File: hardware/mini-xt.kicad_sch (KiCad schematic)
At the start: 0 parts

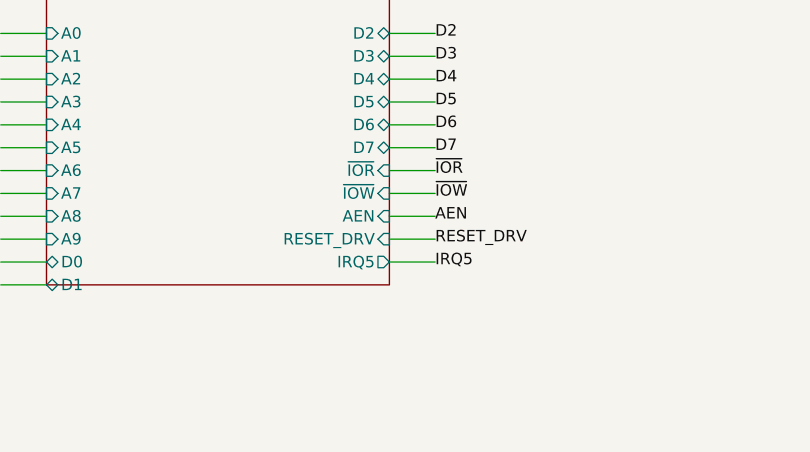
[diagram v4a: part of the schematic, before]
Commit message: Storage: on-board only, IRQ14-default strap; 16-bit IRQ collector
Remove card_storage (same rationale as COM/LPT/RTC -- the on-board sheet
carries the full jumper set; ~25-line wrapper, restorable from git).
Standalone PCBs remaining: video + the isatest jig.

- storage: JP3 IRQ strap -- 1-2 = IRQ14 (DEFAULT, the AT primary-IDE
  convention), 2-3 = IRQ5 (XT fallback; also the LPT alternate), open =
  polled. The '125 now drives STOR_IRQ into the strap, so the unselected
  line is untouched.
- bus_mcu: IRQ14 had no physical path into the soft-PIC, so the IRQ
  collector is now a cascaded pair of 74HCT165s (U19 IRQ10-15 -> U12
  IRQ2-9, net IRQ_CAS), with R19-R24 idle pull-downs and C18. Zero GPIO
  cost -- same IRQ_LOAD/IRQ_CLK/IRQ_SER, firmware shifts 16 bits. Also
  un-dangles the IRQ10-15 interface pins the sheet had declared since day
  one. IRQ10-15 are motherboard-internal (the 60-pin header carries only
  IRQ2-8).
- README: XT-IDE moves into the on-board peripherals list (all three
  straps + the shadow-loaded-BIOS note); motherboard is the third board;
  coexistence example now pairs the on-board XT-IDE with a real ISA IDE
  card at 0x320.
- Design doc: 4.3 card list, 10 JP3 strap + XTIDE UB IRQ-config note
  (was still "Poll or IRQ5"), 5.2 collector row, 14 IRQ table (IRQ14 no
  longer "spare"), 15 BOM row. Decisions logged in open-questions.md,
  questions-storage.md, questions-bus_mcu.md.

Verified: motherboard + both cards rebuild with zero structural ERC;
netlist shows /IRQ14 = {JP3, pull-down, U19 collector input} spanning
storage<->bus_mcu, IRQ_CAS = U19.Q7 -> U12.DS, and /IRQ5 still carrying
sidecar + LPT strap + collector.

Co-Authored-By: Claude Fable 5 <noreply@anthropic.com>
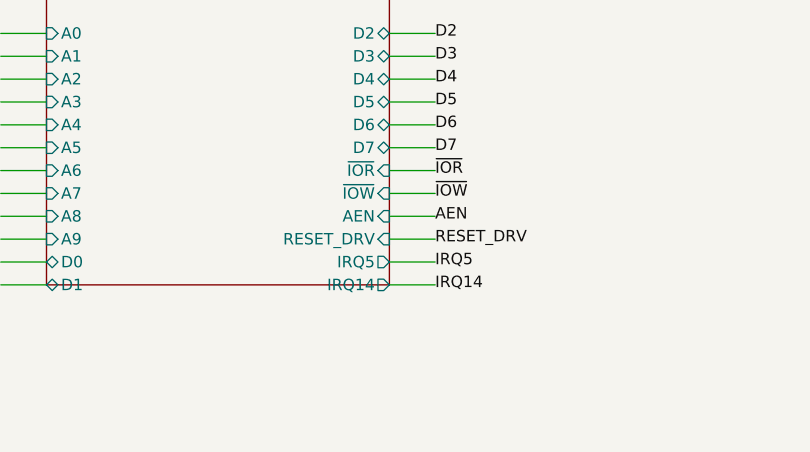
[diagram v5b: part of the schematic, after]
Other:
- sheet STORAGE ports: added IRQ14; removed none
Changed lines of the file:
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@@
 			)
 		)
+		(pin "IRQ14" output
+			(at 158.75 205.74 0)
+			(effects
+				(font
+					(size 1.27 1.27)
+				)
+				(justify left)
+			)
+		)
 		(instances
 			(project "mini-xt"
@@
 		(effects
 			(font
+				(size 1.27 1.27)
+			)
+			(justify left)
+		)
+	)
+	(wire
+		(pts
+			(xy 158.75 205.74)
+			(xy 163.83 205.74)
+		)
+		(stroke
+			(width 0)
+			(type default)
+		)
+	)
+	(label "IRQ14"
+		(at 163.83 205.74 0)
+		(effects
+			(font

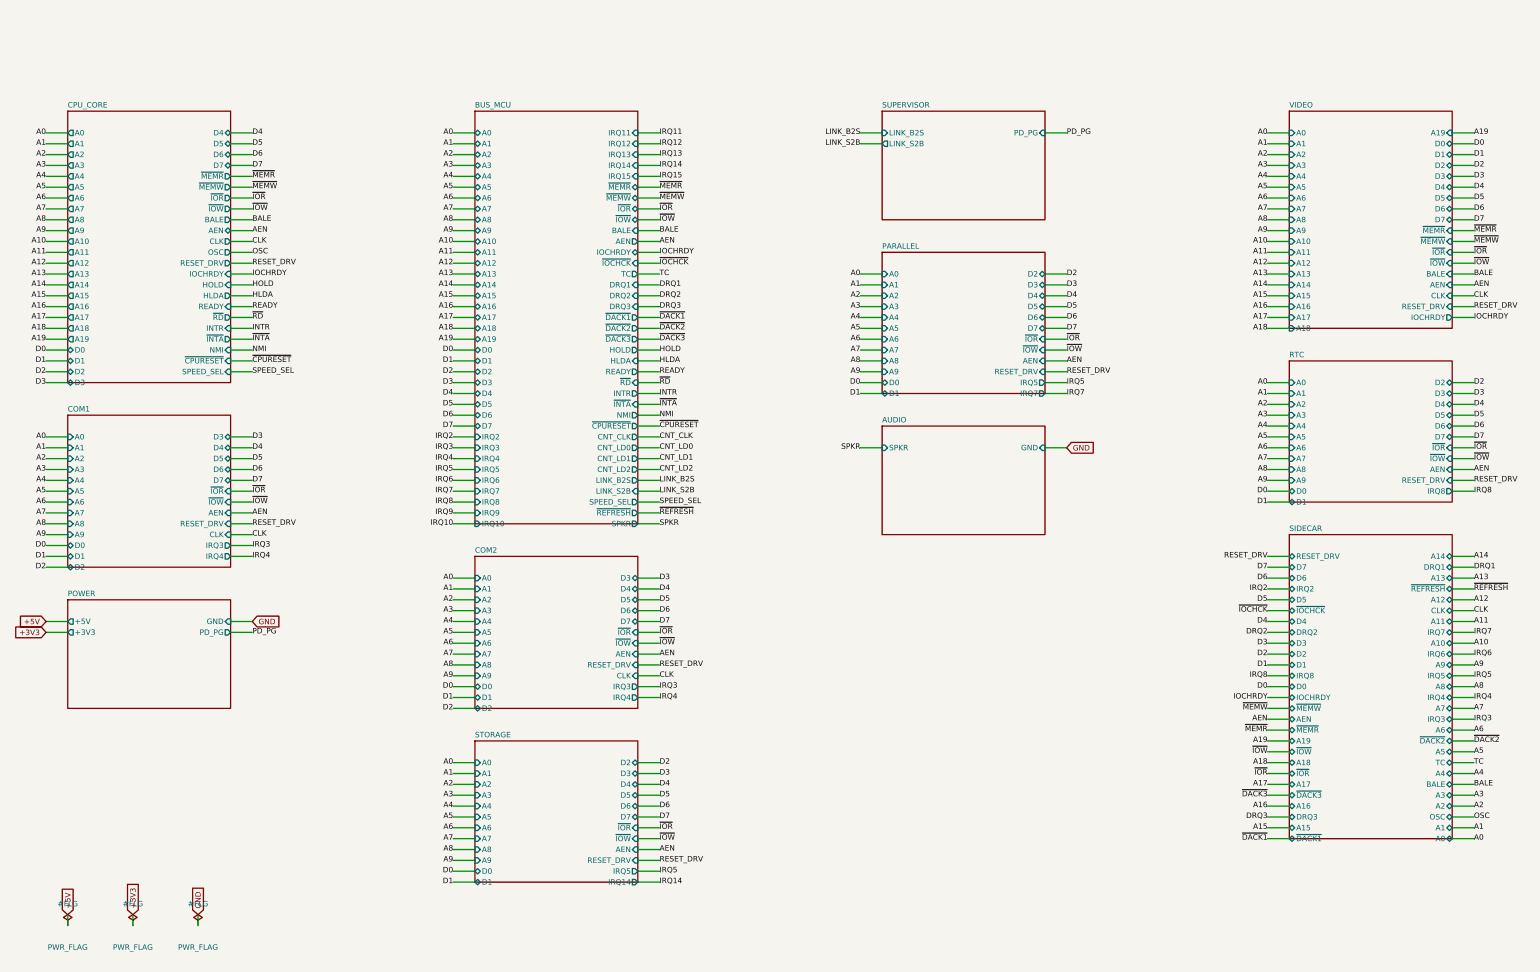
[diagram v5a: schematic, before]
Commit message: PicoGUS on-board: chip-down transcription + shared RP2040 programming port
New picogus sheet (bank 13): a pin-faithful copy of polpo's PicoGUS 2.0
chip-down design (CERN-OHL-P, picogus/hw-chipdown sources) running STOCK
firmware -- the RP2040 GPIO map was extracted from the reference netlist
and our netlist matches it 30-for-30. Copied verbatim: the ADS-muxed
shared AD0-AD7 bus through SN74CB3T FET switches, the ~BUSOE power-up
latch (bus switches off until firmware first toggles ADS), AEN.DACK
IOR/IOW masking, open-drain IOCHRDY, APS6404L-3SQR sample PSRAM, PCM5102A
I2S DAC, IRQ/DMA jumper block (DMA must be jumpered to ch1, the only
MCU-serviced channel; IRQ5 is free since storage moved to IRQ14), AMS1117
local 3V3 island with ferrite-split AVDD/AGND, GPIO29-grounded board
detect, BOOTSEL + LED.

Deviations from the reference (user decisions, logged in
questions-picogus.md): no USB-A gameport (Supervisor owns HID; 0x201
unused), no wavetable header and no MIDI-out jack (build simplification --
the M62429 volume chip and passive mix node went with them; the firmware's
RV_CLK/RV_DATA/MIDI_TX pins are documented no-connects), no local audio
jack (RC-filtered DAC output leaves as PG_L/PG_R into the audio summer ->
the board's one line-out), no local programming USB.

Supervisor: crystal corrected to 30pF + 1k XOUT (same 12MHz part both
RP2040s -- fewer line items), BOOTSEL button added, and J6/SW2 form ONE
USB-C programming port for both bare RP2040s (DPDT slide: A = Supervisor,
C = PicoGUS; KiCad's SW_Slide_DPDT commons are the middle B pins -- the
first draft wired C as common and was corrected). J6 VBUS is unconnected:
the board must be powered to flash, so no back-power path exists.
PGUS_USB_DP/DM are a documented soft-card isolation exception (mxbus
PRIV_PROG); lifting the card means deleting them and fitting a connector.

Audio sheet: J1 line-in stub replaced by PG_L/PG_R interface pins.

Toolchain: six new flat symbols (CB3T3257/CB3T3245/74LVC2G06/PCM5102A/
M62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
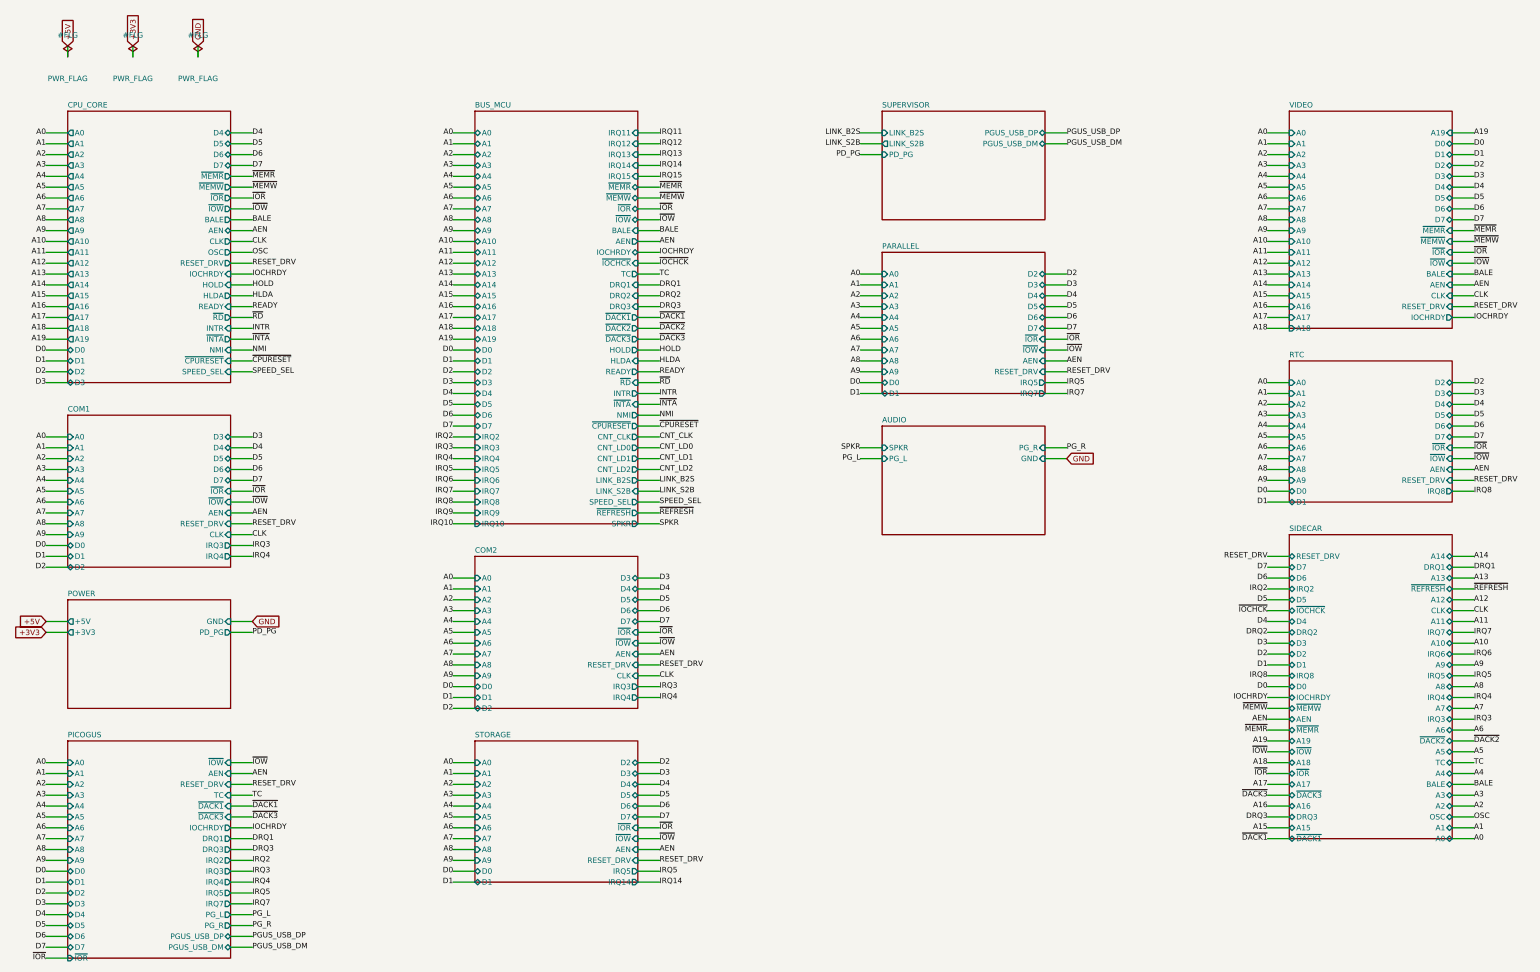
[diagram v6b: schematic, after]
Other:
- added sheet PICOGUS (sheets/picogus.kicad_sch)
- sheet AUDIO ports: added PG_L, PG_R; removed none
- sheet SUPERVISOR ports: added PGUS_USB_DM, PGUS_USB_DP; removed none

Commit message: Design-review fixes: reset parking, IRQ8 off the header, analog cleanups
Netlist-wide review sweep. IRQ8 leaves the 60-pin ISA header (pin 15 is a
second GND return; the on-board RTC owns IRQ8 exclusively, so its push-pull
drive is now correct by construction). Bus MCU Hi-Z parking completed:
~CPURESET pulled low (V20 held in reset while the MCU is unprogrammed),
~DACK1/~REFRESH parked deasserted, DRQ1 idled low. Supervisor 12 MHz crystal
damping R actually in series now (was parallel-to-nothing), plus a second
USBLC6 so both prog-port SW2 positions are ESD-protected. Audio: 0.5x PG
summing (MCP6002 headroom), 100k LINE bleed, unit B parked as a follower --
and the SUM stub moved off pin 5's row, where wiring unit B would have
silently merged SUM into VREF. CH224K VDD fed through 1k per the WCH ref
design. VGA blue ladder rescaled 1k/510 -> 820/470 (was ~12% blue-deficient).
Spare CMOS gate inputs grounded uniformly (cpu_core/rtc/storage); UART_RXD
pulled up (SIN idles at mark with JP1 open); dead pins/parts dropped
(com_port CLK, parallel RESET_DRV, storage R3). Bus CLK fixed at 7.16 MHz
logged as a decision. New passives mapped to JLC basic parts in parts.py.

Co-Authored-By: Claude Fable 5 <noreply@anthropic.com>
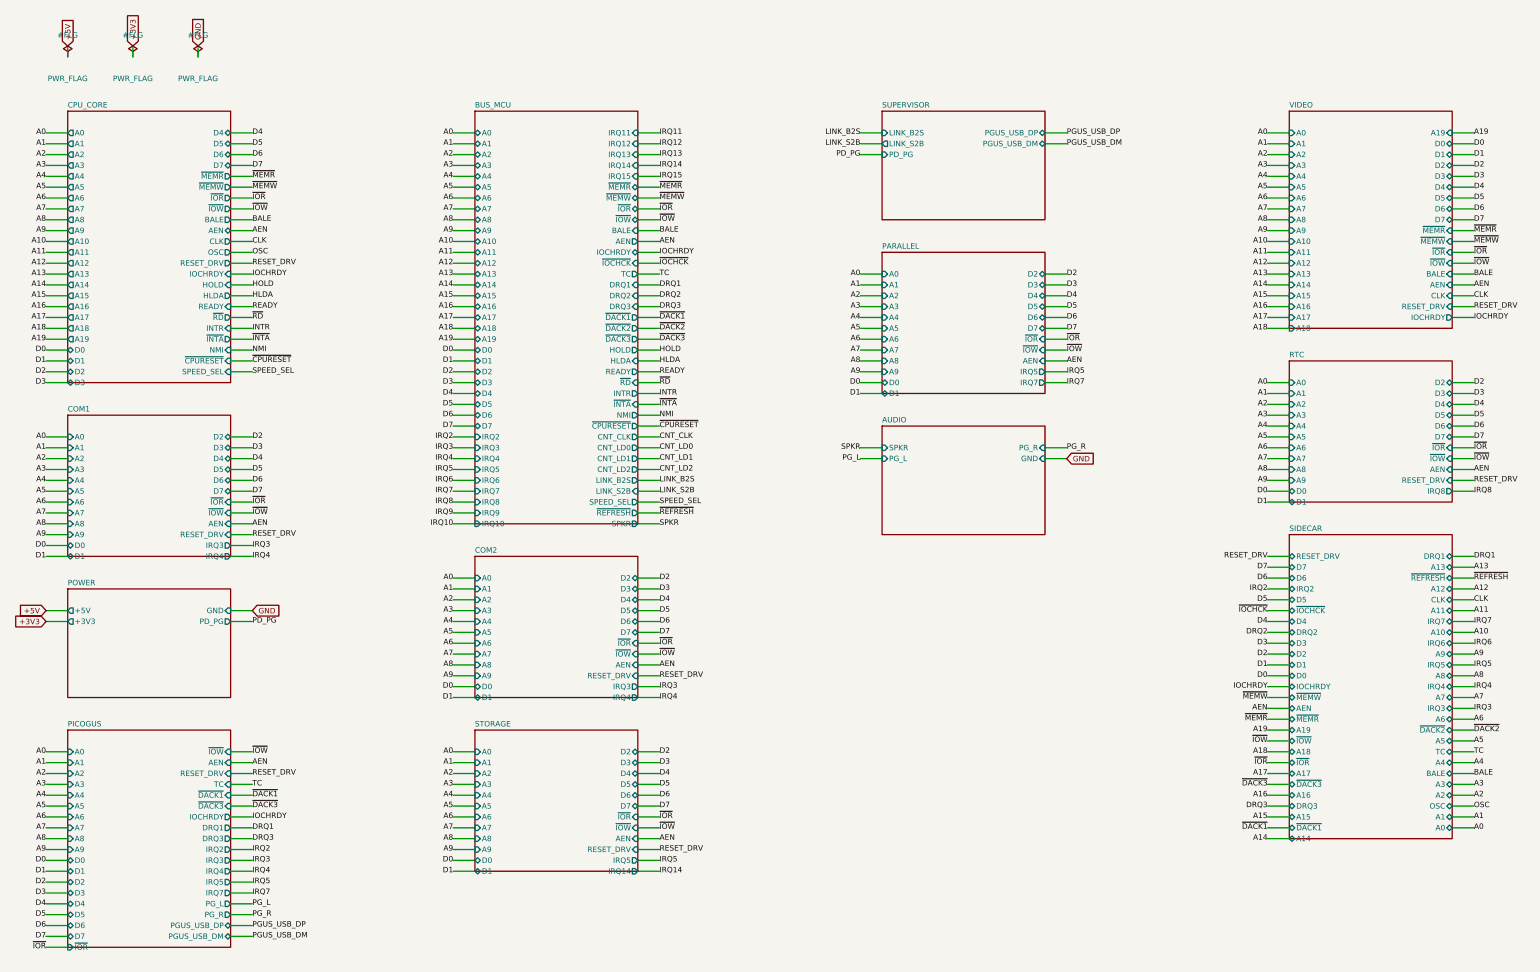
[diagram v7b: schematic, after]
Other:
- sheet COM1 ports: added none; removed CLK
- sheet COM2 ports: added none; removed CLK
- sheet PARALLEL ports: added none; removed RESET_DRV
- sheet SIDECAR ports: added none; removed IRQ8

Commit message: ERC cleanup: NC flags on unused pins, anchored interface labels
KiCad 10 ERC drops from 366 to 16 violations, all noise:

- NC flags on the 36 genuinely unused pins (cpu_core '138/'161 spares,
  Supervisor RP2040 unused GPIO, Core2350B GPIO44-47, rtc '138 spares).
- emit_interface anchors every hier label on a stub wire ending in a
  same-name local label -- connectivity unchanged (still by name;
  netlist spans verified), but nothing dangles.
- Interface honesty: cpu_core drops AEN/IOCHRDY from PINS (both live on
  bus_mcu; nothing here touched them), bus_mcu drops PRIV_COUNTER (the
  counter chain is on-sheet, CNT_* never crosses).
- Remaining 6 label_dangling are root IRQ9-13/15: single-sheet by
  design (soft-PIC pull-ups await future 16-bit sources); kept in PINS
  as the AT-style contract.

Co-Authored-By: Claude Fable 5 <noreply@anthropic.com>
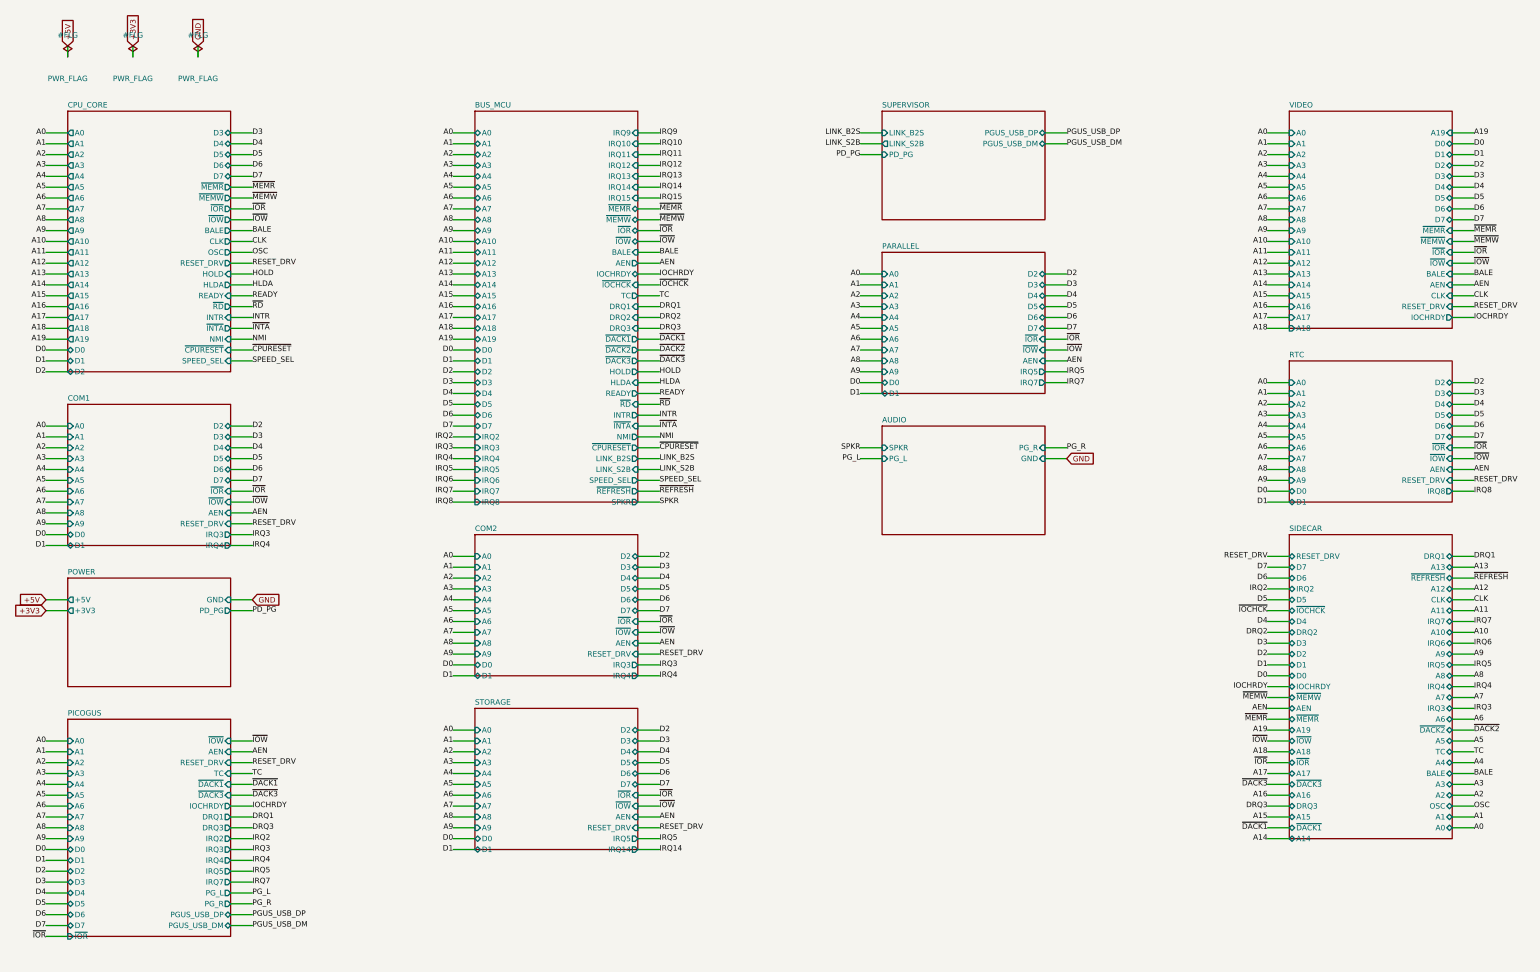
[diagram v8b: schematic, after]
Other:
- sheet BUS_MCU ports: added none; removed CNT_CLK, CNT_LD0, CNT_LD1, CNT_LD2
- sheet CPU_CORE ports: added none; removed AEN, IOCHRDY
